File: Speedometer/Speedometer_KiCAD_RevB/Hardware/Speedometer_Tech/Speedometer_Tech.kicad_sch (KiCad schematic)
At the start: 23 parts, among them P001 3P-SMD/THT

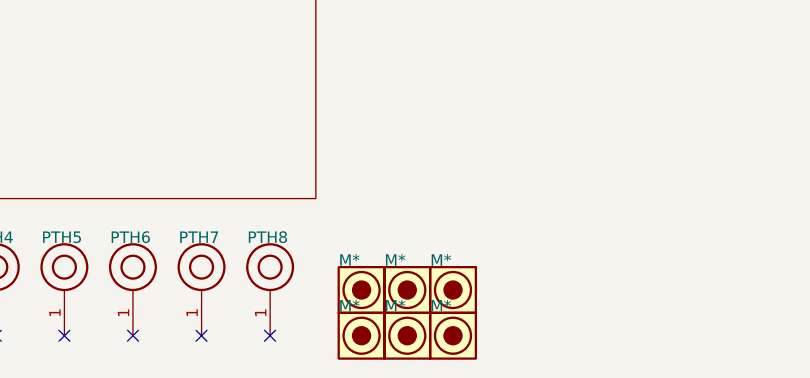
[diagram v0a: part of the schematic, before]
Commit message: updated troq display with new neopixel
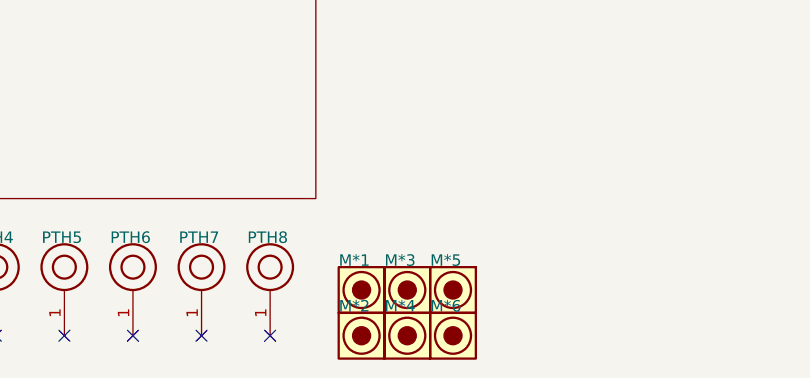
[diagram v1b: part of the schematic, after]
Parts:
- renumbered M* to M*1, M* to M*2, M* to M*3, M* to M*4, M* to M*5, M* to M*6
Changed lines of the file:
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@@
 (kicad_sch
-	(version 20231120)
+	(version 20250114)
 	(generator "eeschema")
-	(generator_version "8.0")
+	(generator_version "9.0")
 	(paper "A3")
+	(rectangle
+		(start 335.28 35.3822)
+		(end 71.12 119.2022)
+		(stroke
+			(width 0.254)
+			(type solid)
+			(color 0 0 0 1)
+		)
+		(fill
+			(type color)
+			(color 255 255 176 1)
+		)
+	)
+	(text "LADA Niva"
+		(exclude_from_sim no)
+		(at 127 50.6222 0)
+		(effects
+			(font
+				(size 4.572 4.572)
+			)
+			(justify left bottom)
+		)
+	)
+	(text "Masse"
+		(exclude_from_sim no)
+		(at 33.02 286.8422 0)
+		(effects
+			(font
+				(size 1.27 1.27)
+			)
+			(justify left bottom)
+		)
+	)
+	(text "4x4 Electric"
+		(exclude_from_sim no)
+		(at 152.4 58.2422 0)
+		(effects
+			(font
+				(size 3.048 3.048)
+			)
+			(justify left bottom)
+		)
+	)
+	(text "Dauerplus"
+		(exclude_from_sim no)
+		(at 33.02 256.3622 0)
+		(effects
+			(font
+				(size 1.27 1.27)
+			)
+			(justify left bottom)
+		)
+	)
+	(text "Zahrzeug-GND"
+		(exclude_from_sim no)
+		(at 33.02 271.6022 0)
+		(effects
+			(font
+				(size 1.27 1.27)
+			)
+			(justify left bottom)
+		)
+	)
 	(junction
 		(at 205.74 76.0222)
@@
 		)
 	)
-	(rectangle
-		(start 335.28 35.3822)
-		(end 71.12 119.2022)
-		(stroke
-			(width 0.254)
-			(type solid)
-			(color 0 0 0 1)
-		)
-		(fill
-			(type color)
-			(color 255 255 176 1)
-		)
-	)
-	(text "LADA Niva"
-		(exclude_from_sim no)
-		(at 127 50.6222 0)
-		(effects
-			(font
-				(size 4.572 4.572)
-			)
-			(justify left bottom)
-		)
-	)
-	(text "Masse"
-		(exclude_from_sim no)
-		(at 33.02 286.8422 0)
-		(effects
-			(font
-				(size 1.27 1.27)
-			)
-			(justify left bottom)
-		)
-	)
-	(text "4x4 Electric"
-		(exclude_from_sim no)
-		(at 152.4 58.2422 0)
-		(effects
-			(font
-				(size 3.048 3.048)
-			)
-			(justify left bottom)
-		)
-	)
-	(text "Dauerplus"
-		(exclude_from_sim no)
-		(at 33.02 256.3622 0)
-		(effects
-			(font
-				(size 1.27 1.27)
-			)
-			(justify left bottom)
-		)
-	)
-	(text "Zahrzeug-GND"
-		(exclude_from_sim no)
-		(at 33.02 271.6022 0)
-		(effects
-			(font
-				(size 1.27 1.27)
-			)
-			(justify left bottom)
-		)
-	)
 	(symbol
 		(lib_id "Speedometer_Tech-altium-import:root_0_PTH-M4D7X7-Symbol-1")
@@
 		(on_board yes)
 		(dnp no)
-		(property "Reference" "M*"
+		(property "Reference" "M*2"
 			(at 281.94 284.3022 0)
 			(effects
@@
 			(project ""
 				(path "/7a911dfa-7957-409a-ad31-10c26a0bf949"
-					(reference "M*")
+					(reference "M*2")
 					(unit 1)
 				)
@@
 		(on_board yes)
 		(dnp no)
-		(property "Reference" "#PWR?"
+		(property "Reference" "#PWR0106"
 			(at 25.4 258.9022 0)
 			(effects
@@
 			(project ""
 				(path "/7a911dfa-7957-409a-ad31-10c26a0bf949"
-					(reference "#PWR?")
+					(reference "#PWR0106")
 					(unit 1)
 				)
@@
 		(on_board yes)
 		(dnp no)
-		(property "Reference" "#PWR?"
+		(property "Reference" "#PWR0101"
 			(at 66.04 65.8622 0)
 			(effects
@@
 			(project ""
 				(path "/7a911dfa-7957-409a-ad31-10c26a0bf949"
-					(reference "#PWR?")
+					(reference "#PWR0101")
 					(unit 1)
 				)
@@
 		(on_board yes)
 		(dnp no)
-		(property "Reference" "#PWR?"
+		(property "Reference" "#PWR0105"
 			(at 25.4 281.7622 0)
 			(effects
@@
 			(project ""
 				(path "/7a911dfa-7957-409a-ad31-10c26a0bf949"
-					(reference "#PWR?")
+					(reference "#PWR0105")
 					(unit 1)
 				)
@@
 		(on_board yes)
 		(dnp no)
-		(property "Reference" "#PWR?"
+		(property "Reference" "#PWR0104"
 			(at 45.72 281.7622 0)
 			(effects
@@
 			(project ""
 				(path "/7a911dfa-7957-409a-ad31-10c26a0bf949"
-					(reference "#PWR?")
+					(reference "#PWR0104")
 					(unit 1)
 				)
@@
 		(on_board yes)
 		(dnp no)
-		(property "Reference" "M*"
+		(property "Reference" "M*4"
 			(at 287.02 284.3022 0)
 			(effects
@@
 			(project ""
 				(path "/7a911dfa-7957-409a-ad31-10c26a0bf949"
-					(reference "M*")
+					(reference "M*4")
 					(unit 1)
 				)
@@
 		(on_board yes)
 		(dnp no)
-		(property "Reference" "M*"
+		(property "Reference" "M*5"
 			(at 292.1 279.2222 0)
 			(effects
@@
 			(project ""
 				(path "/7a911dfa-7957-409a-ad31-10c26a0bf949"
-					(reference "M*")
+					(reference "M*5")
 					(unit 1)
 				)
@@
 		(on_board yes)
 		(dnp no)
-		(property "Reference" "M*"
+		(property "Reference" "M*3"
 			(at 287.02 279.2222 0)
 			(effects
@@
 			(project ""
 				(path "/7a911dfa-7957-409a-ad31-10c26a0bf949"
-					(reference "M*")
+					(reference "M*3")
 					(unit 1)
 				)
@@
 		(on_board yes)
 		(dnp no)
-		(property "Reference" "M*"
+		(property "Reference" "M*1"
 			(at 281.94 279.2222 0)
 			(effects
@@
 			(project ""
 				(path "/7a911dfa-7957-409a-ad31-10c26a0bf949"
-					(reference "M*")
+					(reference "M*1")
 					(unit 1)
 				)
@@
 		(on_board yes)
 		(dnp no)
-		(property "Reference" "M*"
+		(property "Reference" "M*6"
 			(at 292.1 284.3022 0)
 			(effects
@@
 			(project ""
 				(path "/7a911dfa-7957-409a-ad31-10c26a0bf949"
-					(reference "M*")
+					(reference "M*6")
 					(unit 1)
 				)
@@
 		(on_board yes)
 		(dnp no)
-		(property "Reference" "#PWR?"
+		(property "Reference" "#PWR0103"
 			(at 45.72 258.9022 0)
 			(effects
@@
 			(project ""
 				(path "/7a911dfa-7957-409a-ad31-10c26a0bf949"
-					(reference "#PWR?")
+					(reference "#PWR0103")
 					(unit 1)
 				)
@@
 		(on_board yes)
 		(dnp no)
-		(property "Reference" "#PWR?"
+		(property "Reference" "#PWR0102"
 			(at 66.04 60.7822 0)
 			(effects
@@
 			(project ""
 				(path "/7a911dfa-7957-409a-ad31-10c26a0bf949"
-					(reference "#PWR?")
+					(reference "#PWR0102")
 					(unit 1)
 				)
@@
 		(at 152.4 182.7022)
 		(size 25.4 50.8)
+		(exclude_from_sim no)
+		(in_bom yes)
+		(on_board yes)
+		(dnp no)
 		(fields_autoplaced yes)
 		(stroke
@@
 		(at 304.8 43.0022)
 		(size 25.4 50.8)
+		(exclude_from_sim no)
+		(in_bom yes)
+		(on_board yes)
+		(dnp no)
 		(fields_autoplaced yes)
 		(stroke
@@
 		(at 88.9 76.0222)
 		(size 12.7 12.7)
+		(exclude_from_sim no)
+		(in_bom yes)
+		(on_board yes)
+		(dnp no)
 		(fields_autoplaced yes)
 		(stroke
@@
 		(at 228.6 68.4022)
 		(size 50.8 25.4)
+		(exclude_from_sim no)
+		(in_bom yes)
+		(on_board yes)
+		(dnp no)
 		(fields_autoplaced yes)
 		(stroke
@@
 		(at 76.2 101.4222)
 		(size 254 12.7)
+		(exclude_from_sim no)
+		(in_bom yes)
+		(on_board yes)
+		(dnp no)
 		(fields_autoplaced yes)
 		(stroke
@@
 		(at 228.6 144.6022)
 		(size 50.8 127)
+		(exclude_from_sim no)
+		(in_bom yes)
+		(on_board yes)
+		(dnp no)
 		(fields_autoplaced yes)
 		(stroke
@@
 		(at 152.4 144.6022)
 		(size 25.4 25.4)
+		(exclude_from_sim no)
+		(in_bom yes)
+		(on_board yes)
+		(dnp no)
 		(fields_autoplaced yes)
 		(stroke
@@
 		(at 127 68.4022)
 		(size 50.8 25.4)
+		(exclude_from_sim no)
+		(in_bom yes)
+		(on_board yes)
+		(dnp no)
 		(fields_autoplaced yes)
 		(stroke
@@
 		(at 203.2 43.0022)
 		(size 76.2 50.8)
+		(exclude_from_sim no)
+		(in_bom yes)
+		(on_board yes)
+		(dnp no)
 		(fields_autoplaced yes)
 		(stroke
@@
 		(at 152.4 246.2022)
 		(size 25.4 25.4)
+		(exclude_from_sim no)
+		(in_bom yes)
+		(on_board yes)
+		(dnp no)
 		(fields_autoplaced yes)
 		(stroke
@@
 		(at 76.2 43.0022)
 		(size 25.4 50.8)
+		(exclude_from_sim no)
+		(in_bom yes)
+		(on_board yes)
+		(dnp no)
 		(fields_autoplaced yes)
 		(stroke
@@
 		)
 	)
+	(embedded_fonts no)
 )

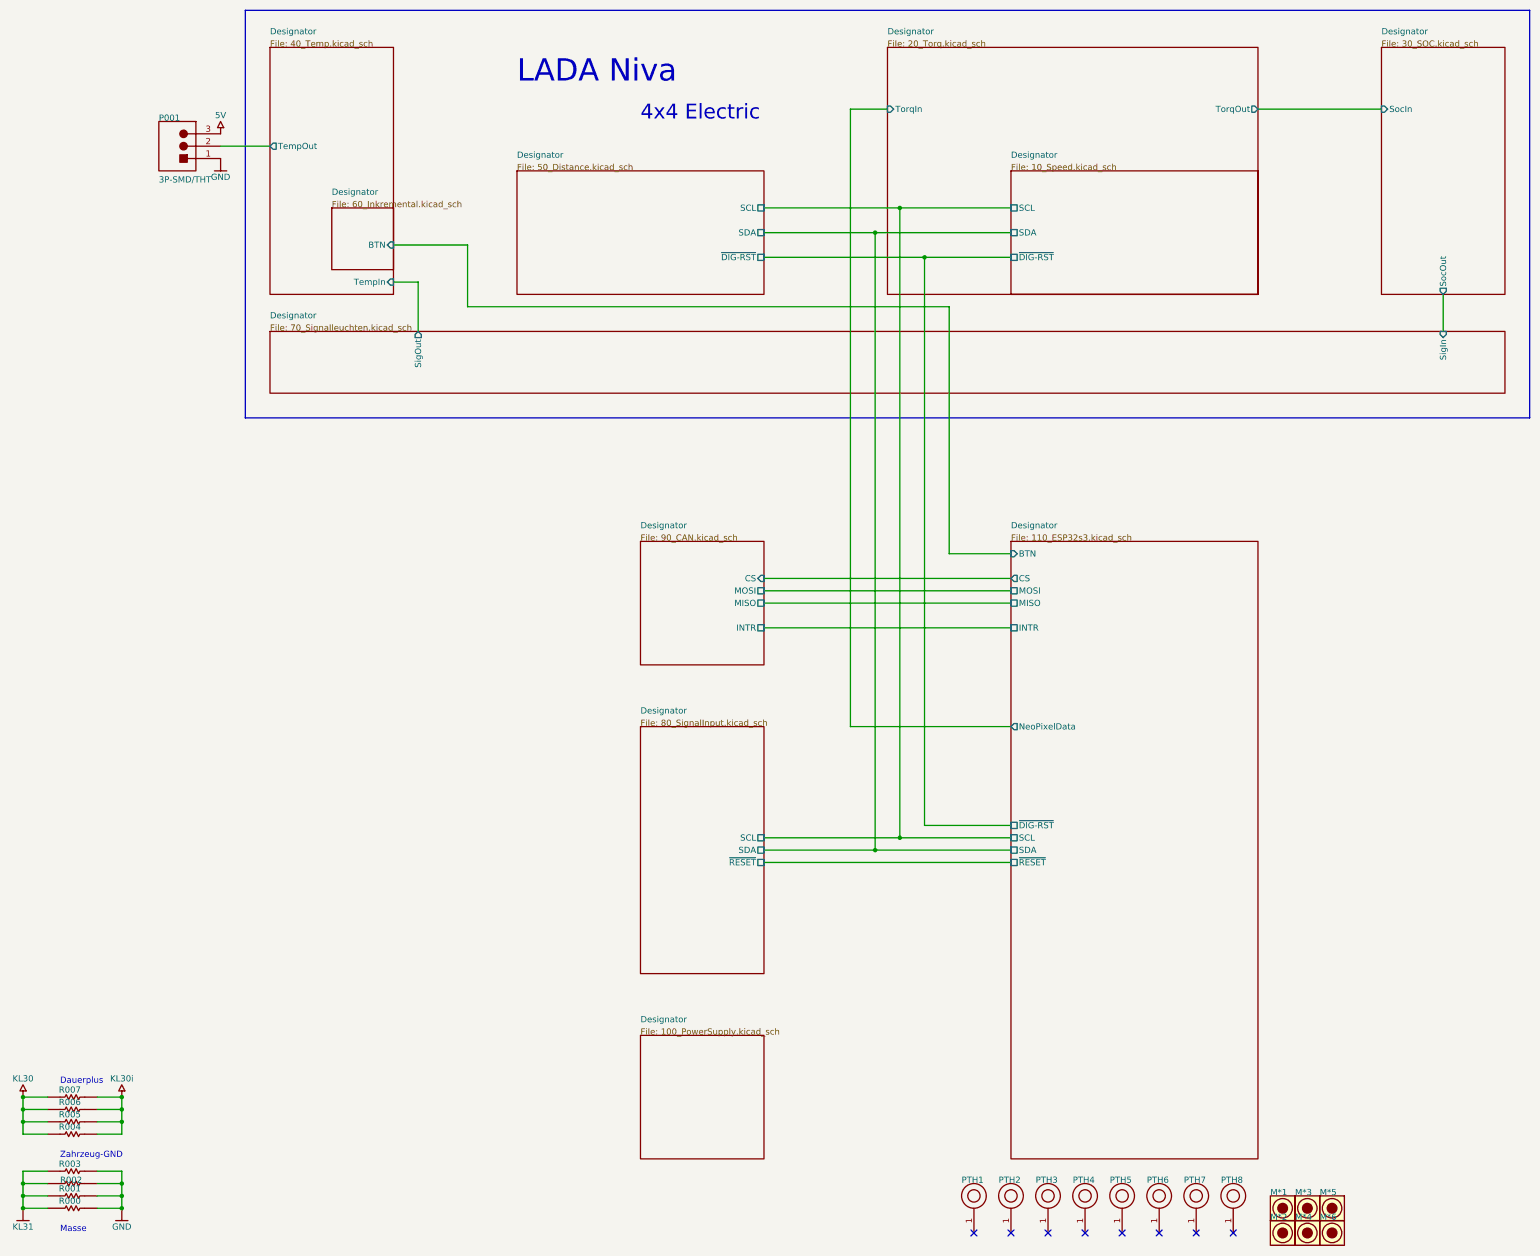
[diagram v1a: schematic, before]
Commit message: current version of lada speedometer in kicad
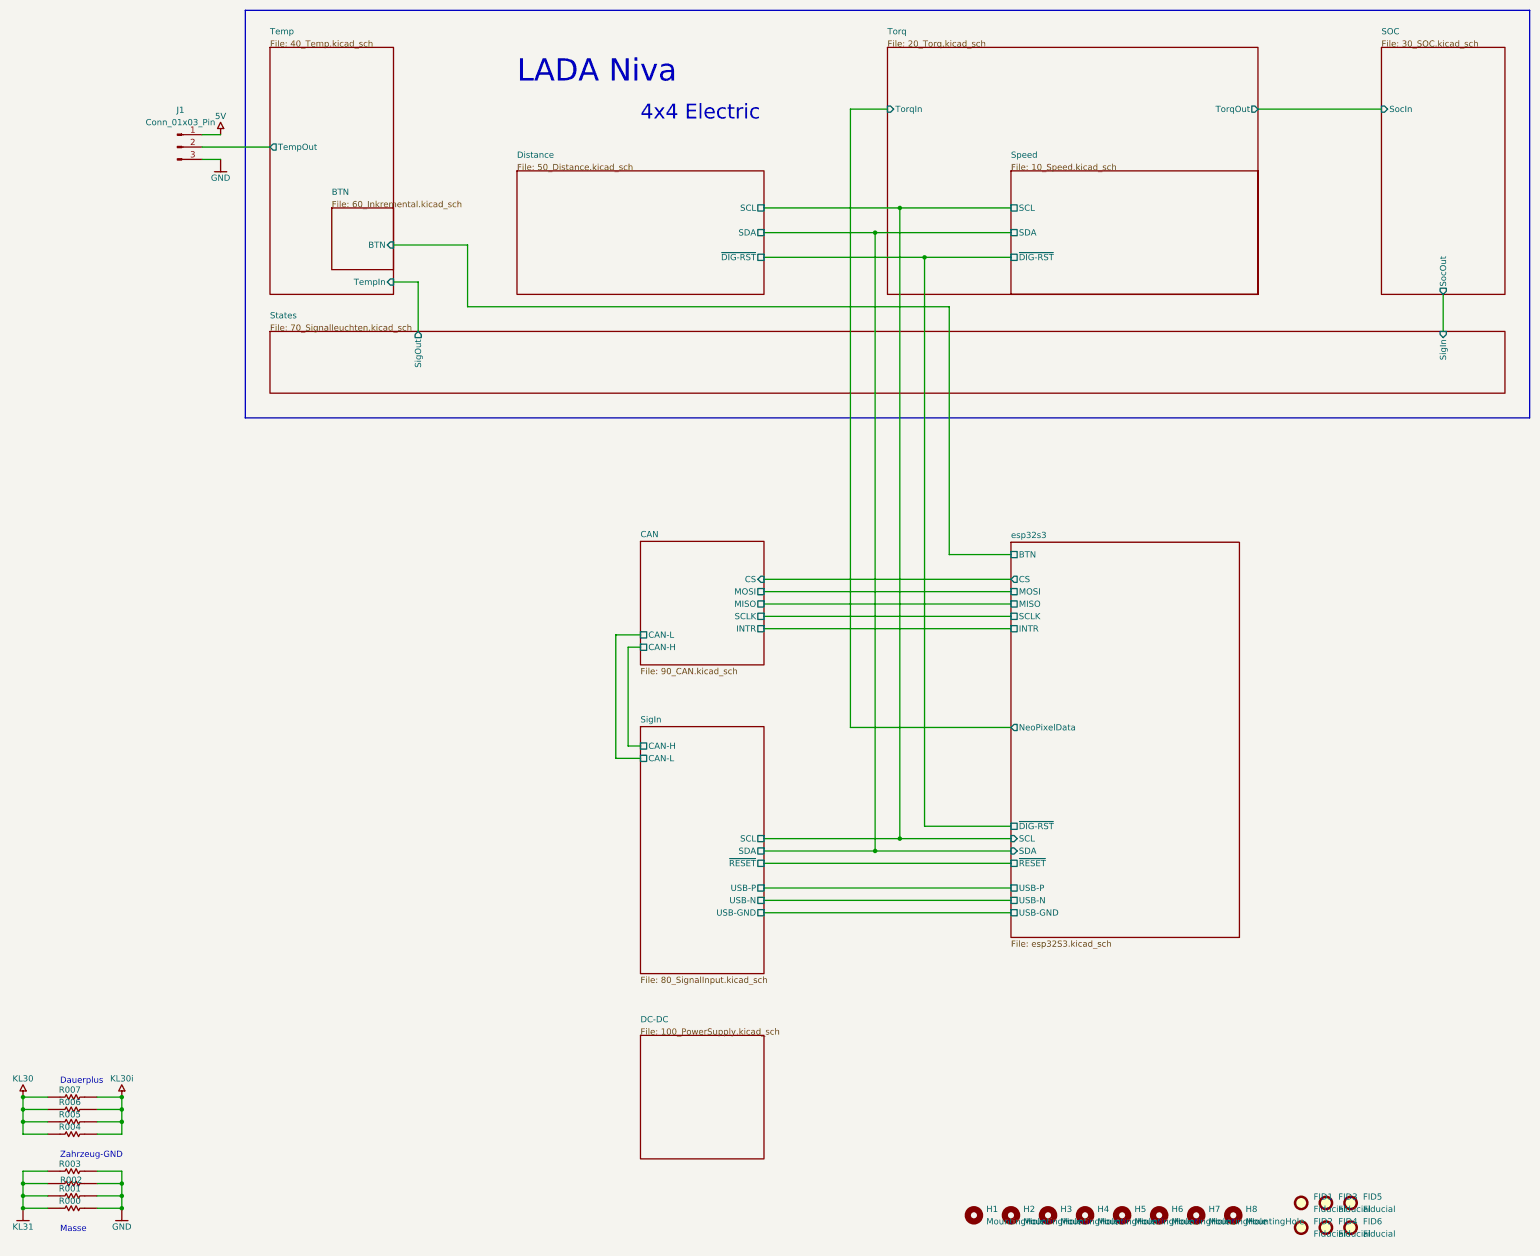
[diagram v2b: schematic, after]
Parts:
- removed M*1, M*2, M*3, M*4, M*5, M*6: Passermarke, Passermarke-Footprint-1, symbol Speedometer_Tech-altium-import:root_0_Passermarke-Symbol-1
- removed P001: 3P-SMD/THT, 3P-SMD/THT, symbol Speedometer_Tech-altium-import:root_2_3P-SMD/THT
- removed PTH1, PTH2, PTH3, PTH4, PTH5, PTH6, PTH7, PTH8: PTH-M4D7X7, PTH-M4D7X7-Footprint-1, symbol Speedometer_Tech-altium-import:root_0_PTH-M4D7X7-Symbol-1
- added FID1, FID2, FID3, FID4, FID5, FID6: Fiducial, Fiducial:Fiducial_0.5mm_Mask1mm, symbol Mechanical:Fiducial
- added H1, H2, H3, H4, H5, H6, H7, H8: MountingHole, MountingHole:MountingHole_4.3mm_M4_ISO7380, symbol Mechanical:MountingHole
- added J1: Conn_01x03_Pin, Connector_PinHeader_2.54mm:PinHeader_1x03_P2.54mm_Horizontal, symbol Connector:Conn_01x03_Pin
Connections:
- net 5V: now also J1.1 (Pin_1)
- net Temp/TempOut: now also J1.2 (Pin_2)
- net GND: now also J1.3 (Pin_3)
- no-connect marks 8 -> 0
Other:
- sheet Designator renamed Temp
- added sheet BTN (60_Inkremental.kicad_sch)
- added sheet CAN (90_CAN.kicad_sch)
- added sheet DC-DC (100_PowerSupply.kicad_sch)
- added sheet Distance (50_Distance.kicad_sch)
- added sheet SOC (30_SOC.kicad_sch)
- added sheet SigIn (80_SignalInput.kicad_sch)
- added sheet Speed (10_Speed.kicad_sch)
- added sheet States (70_Signalleuchten.kicad_sch)
- added sheet Torq (20_Torq.kicad_sch)
- added sheet esp32s3 (esp32S3.kicad_sch)

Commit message: Speedometer DRC mostly passed
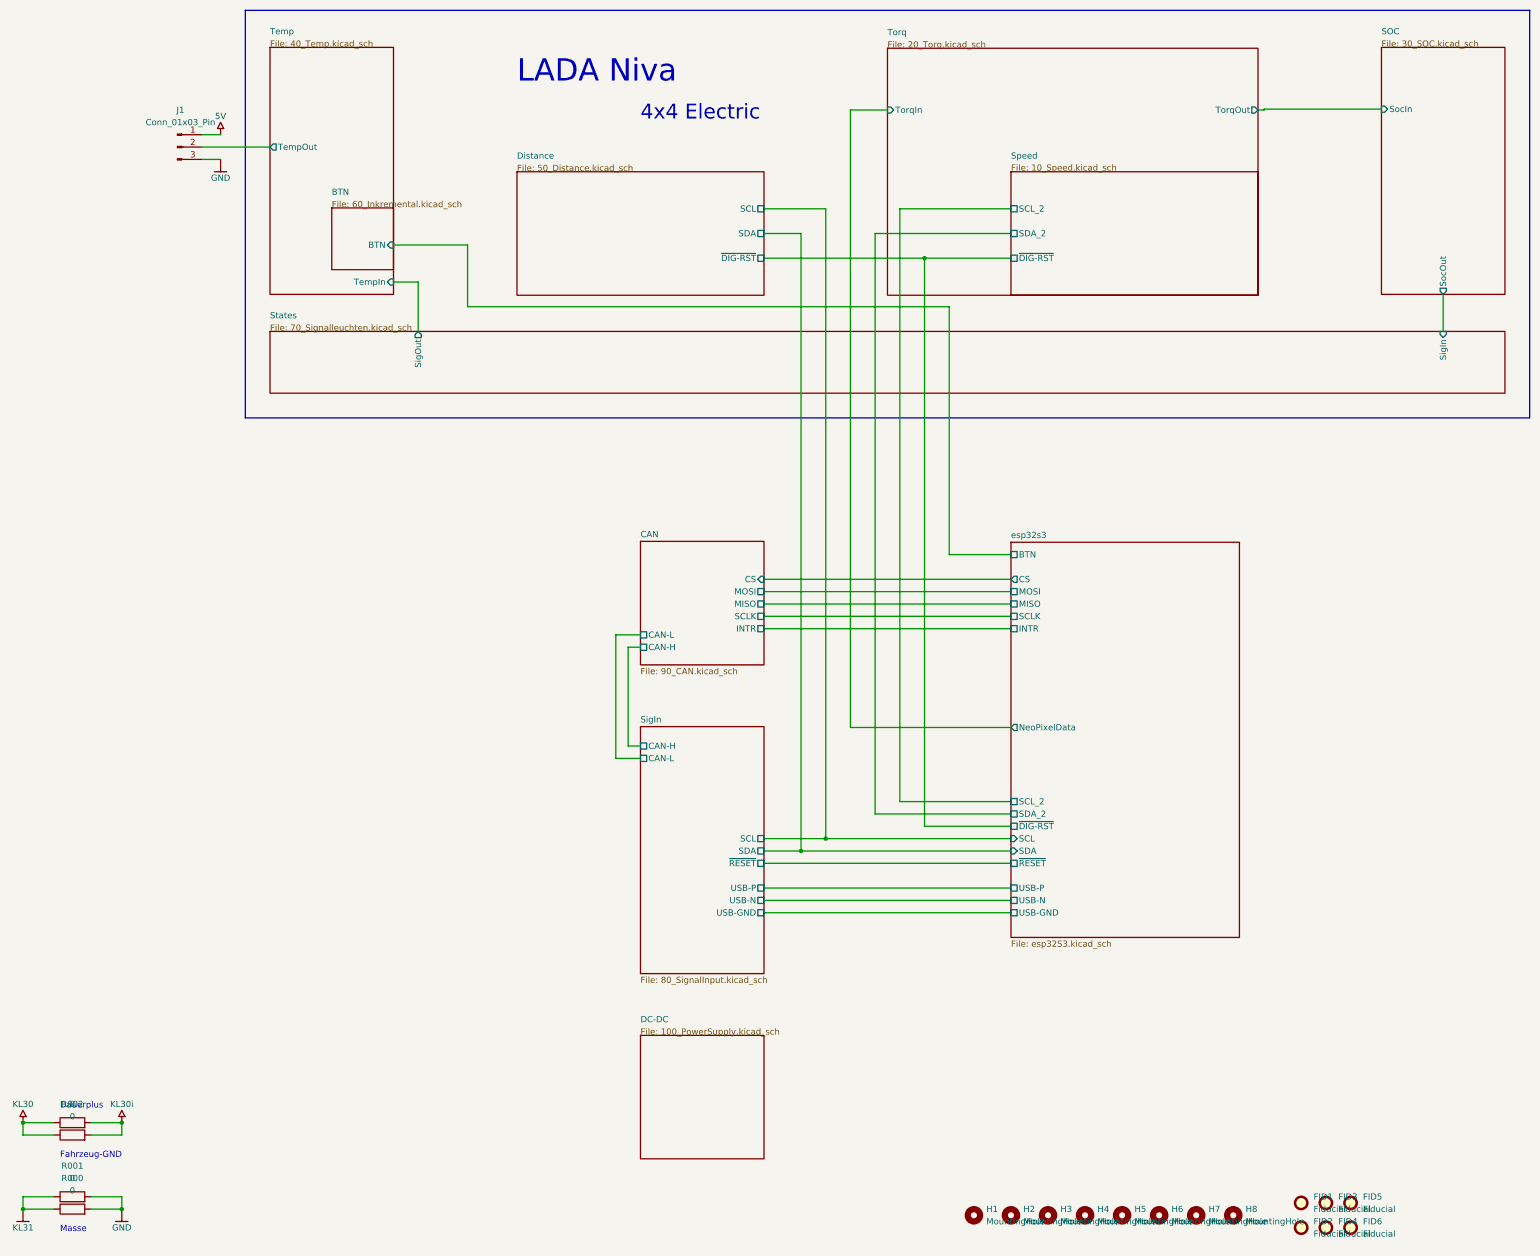
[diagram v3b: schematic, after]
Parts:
- removed R000, R001, R002, R003, R004, R005, R006, R007: RC0603JR-070RL, RESC1608X55X25ML10T15, symbol Speedometer_Tech-altium-import:root_0_RES-2
- added R000, R001, R002, R003: 0, Resistor_SMD:R_0603_1608Metric, symbol Device:R
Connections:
- net GND: now also R000.2, R001.2
- net KL30: now also R002.1, R003.1
- net KL30i: now also R002.2, R003.2
- net KL31: now also R000.1, R001.1
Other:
- sheet Speed ports: added SCL_2, SDA_2; removed SCL, SDA
- sheet esp32s3 ports: added SCL_2, SDA_2; removed none
- note added: "Fahrzeug-GND"
- note removed: "Zahrzeug-GND"
